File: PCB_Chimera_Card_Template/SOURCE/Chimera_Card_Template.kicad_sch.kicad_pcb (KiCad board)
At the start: 4 copper layers, 24 x 56 mm, 8 parts, among them CN1 NASB0-S6701-TS50

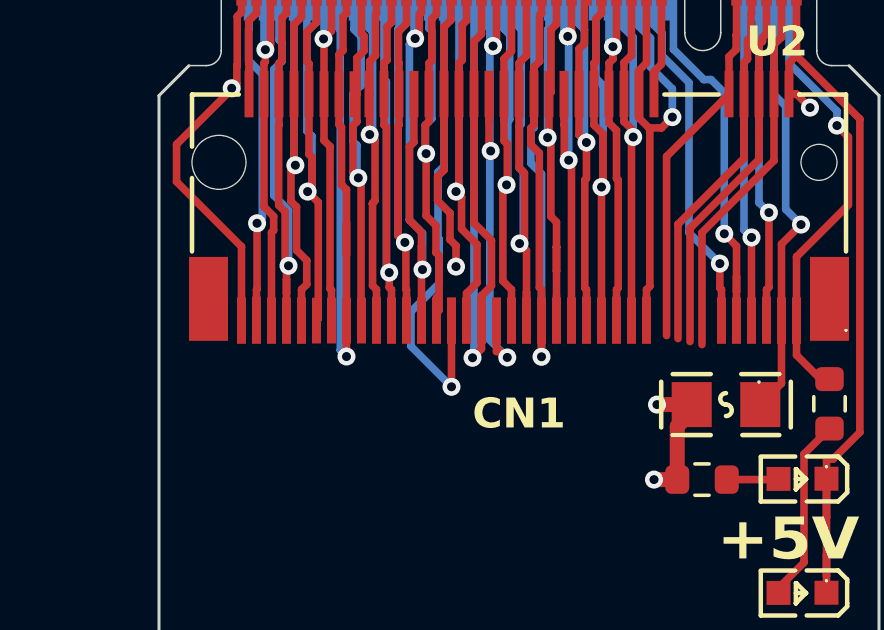
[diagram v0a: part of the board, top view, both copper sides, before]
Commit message: Connected air wire on pad 47 of the card_template
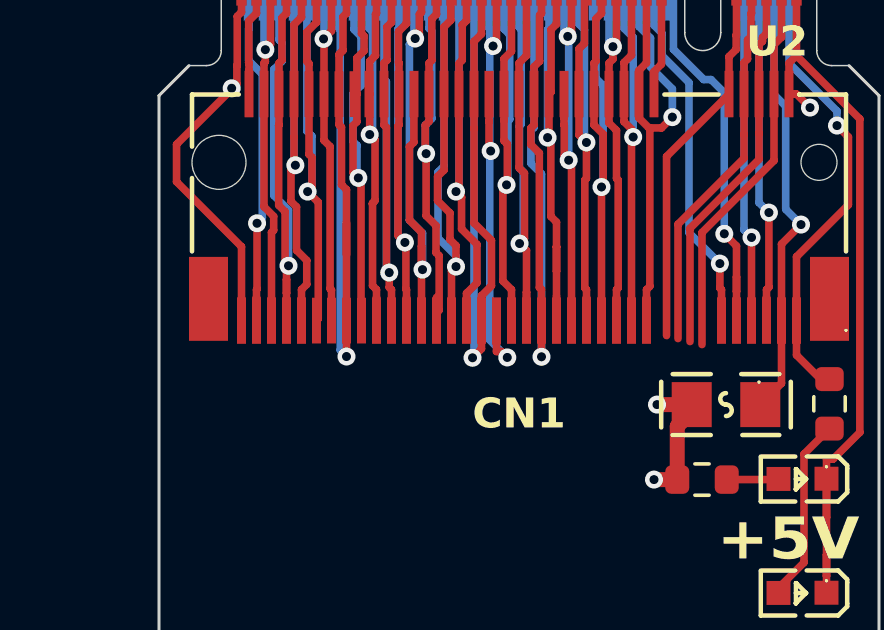
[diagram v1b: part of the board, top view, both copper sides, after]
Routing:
- net Net-(CN1-20-Pad47): track 29.6 -> 21.2 mm, vias 2 -> 1
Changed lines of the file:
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@@
   (segment (start 16.4998 -55.0965) (end 16.4998 -55.0499) (width 0.1524) (layer "F.Cu") (net 41))
   (segment (start 9.727 -58.702) (end 9.727 -57.512615) (width 0.254) (layer "F.Cu") (net 42))
-  (segment (start 9.75 -47.5) (end 9.75 -45.2929) (width 0.254) (layer "F.Cu") (net 42))
   (segment (start 9.75 -58.725) (end 9.727 -58.702) (width 0.254) (layer "F.Cu") (net 42))
+  (segment (start 9.9 -49.3) (end 9.749964 -49.149964) (width 0.254) (layer "F.Cu") (net 42))
   (segment (start 9.7 -50.2) (end 9.9 -50) (width 0.254) (layer "F.Cu") (net 42))
   (segment (start 9.285 -51.5) (end 9.7 -51.085) (width 0.254) (layer "F.Cu") (net 42))
@@
   (segment (start 9.7 -51.085) (end 9.7 -50.2) (width 0.254) (layer "F.Cu") (net 42))
   (segment (start 9.499773 -52.514773) (end 9.285 -52.3) (width 0.254) (layer "F.Cu") (net 42))
+  (segment (start 9.749964 -49.149964) (end 9.749964 -47.499971) (width 0.254) (layer "F.Cu") (net 42))
   (segment (start 9.9 -50) (end 9.9 -49.3) (width 0.254) (layer "F.Cu") (net 42))
   (segment (start 9.727 -57.512615) (end 9.499773 -57.285388) (width 0.254) (layer "F.Cu") (net 42))
-  (via (at 9.75 -45.2929) (size 0.6) (drill 0.3) (layers "F.Cu" "B.Cu") (net 42))
   (via (at 9.9 -49.3) (size 0.6) (drill 0.3) (layers "F.Cu" "B.Cu") (net 42))
   (segment (start 9.9 -49.3) (end 9.897 -49.297) (width 0.254) (layer "In1.Cu") (net 42))
-  (segment (start 9.897 -49.297) (end 9.897 -46.003) (width 0.254) (layer "In1.Cu") (net 42))
+  (segment (start 9.9 -49.652375) (end 9.9 -49.3) (width 0.254) (layer "B.Cu") (net 42))
   (segment (start 9.5 -52.649575) (end 9.3 -52.449575) (width 0.254) (layer "B.Cu") (net 42))
-  (segment (start 8.4 -47.8) (end 8.4 -46.6429) (width 0.254) (layer "B.Cu") (net 42))
   (segment (start 9.3 -52.449575) (end 9.3 -50.252375) (width 0.254) (layer "B.Cu") (net 42))
-  (segment (start 9.34 -50.212375) (end 9.34 -48.74) (width 0.254) (layer "B.Cu") (net 42))
+  (segment (start 9.3 -50.252375) (end 9.9 -49.652375) (width 0.254) (layer "B.Cu") (net 42))
   (segment (start 9.5 -58.475) (end 9.5 -52.649575) (width 0.254) (layer "B.Cu") (net 42))
-  (segment (start 9.34 -48.74) (end 8.4 -47.8) (width 0.254) (layer "B.Cu") (net 42))
-  (segment (start 9.3 -50.252375) (end 9.34 -50.212375) (width 0.254) (layer "B.Cu") (net 42))
-  (segment (start 8.4 -46.6429) (end 9.75 -45.2929) (width 0.254) (layer "B.Cu") (net 42))
   (segment (start 20.749964 -45.40747) (end 20.749964 -47.499971) (width 0.254) (layer "F.Cu") (net 43))
   (segment (start 21.4 -50.7) (end 20.75 -50.05) (width 0.254) (layer "F.Cu") (net 43))

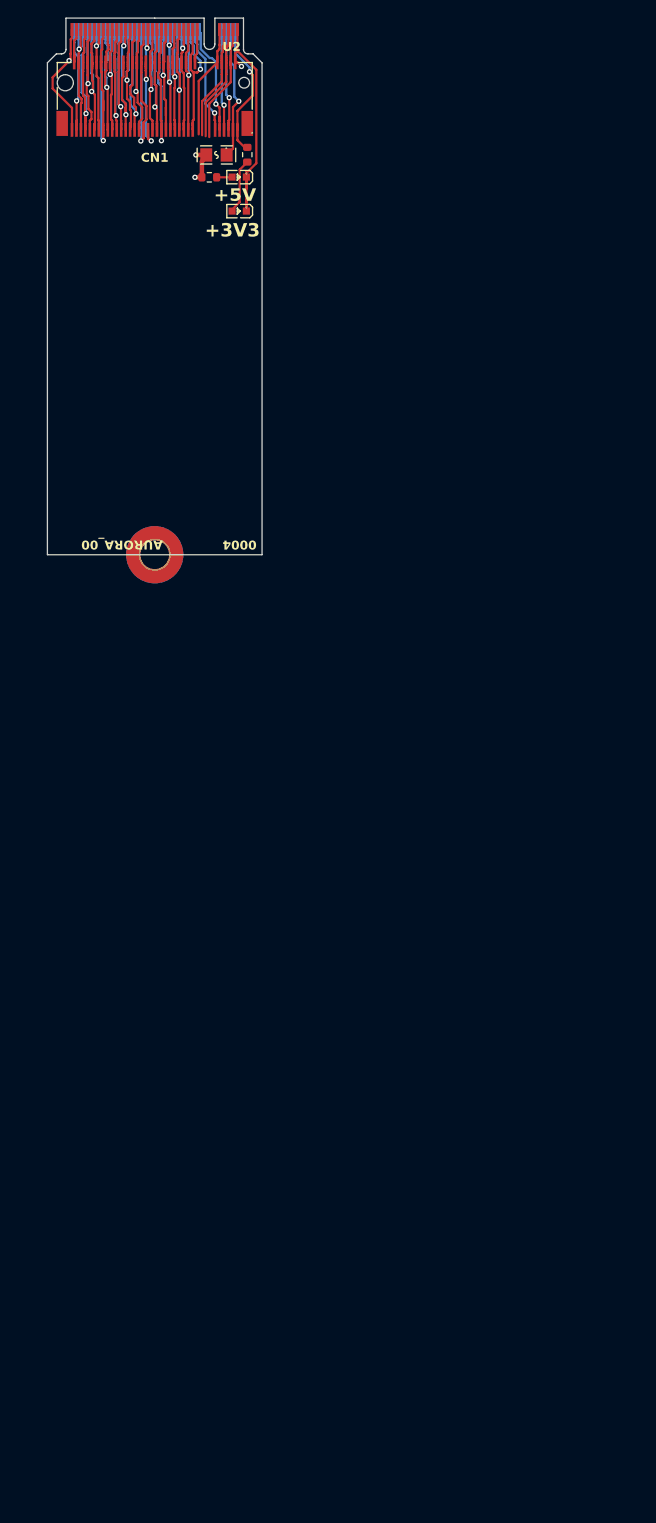
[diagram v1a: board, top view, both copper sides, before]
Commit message: Moved board into title block border. for Chimera_Card_template
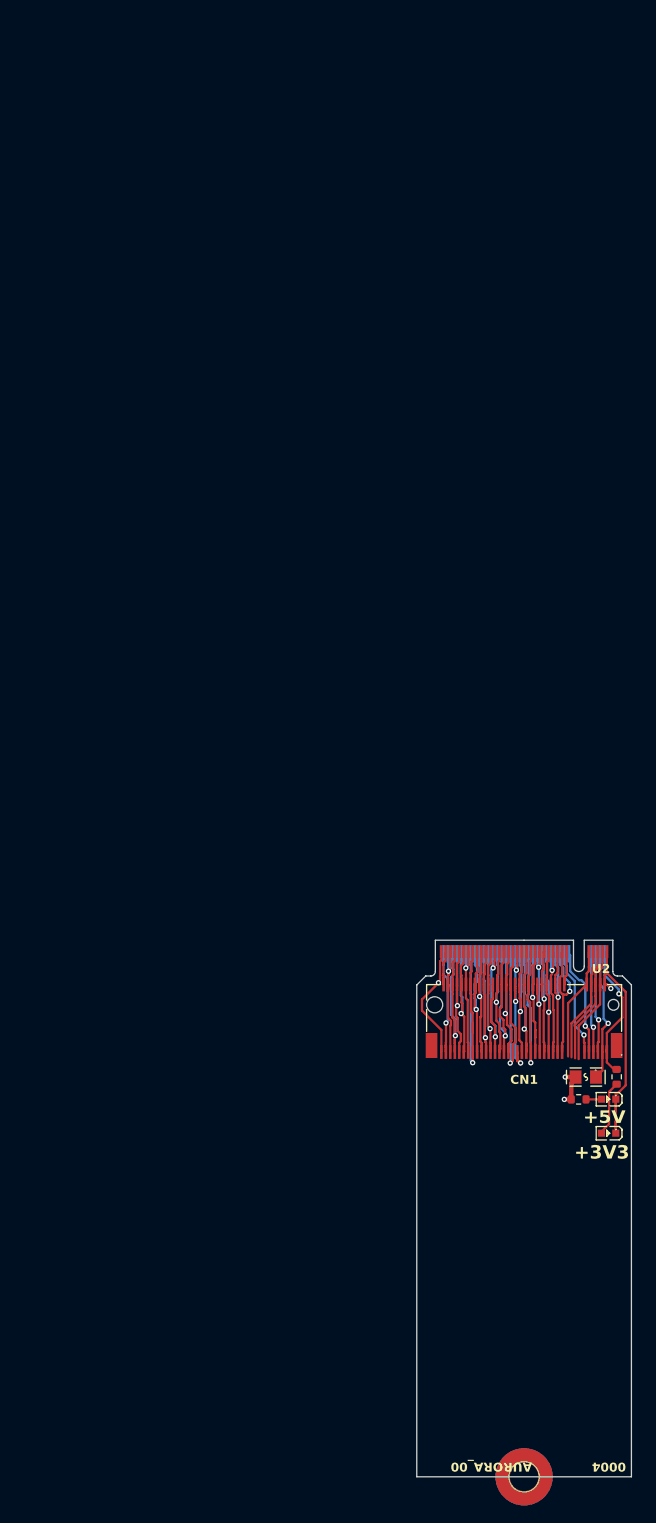
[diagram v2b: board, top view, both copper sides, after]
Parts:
- moved CN1 111.1 mm to (53.3, 51.8)
- moved F1 111.1 mm to (60.2, 58.4)
- moved H1 111.1 mm to (53.3, 103.1)
- moved LED1 111.1 mm to (62.8, 60.9)
- moved LED2 111.1 mm to (62.8, 64.7)
- moved R1 111.1 mm to (63.6, 58.4)
- moved R2 111.1 mm to (59.4, 60.9)
- moved U2 111.1 mm to (53.3, 43.1)
